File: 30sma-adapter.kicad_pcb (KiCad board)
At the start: 4 copper layers, 34 parts, among them J1 Conn_Coaxial, J10 Conn_Coaxial, J11 Conn_Coaxial, J12 Conn_Coaxial, J13 Conn_Coaxial, J14 Conn_Coaxial, J15 Conn_Coaxial, J16 Conn_Coaxial, J17 Conn_Coaxial, J18 Conn_Coaxial, J19 Conn_Coaxial, J2 Conn_Coaxial, J20 Conn_Coaxial, J21 Conn_Coaxial, J22 Conn_Coaxial, J23 Conn_Coaxial, J24 Conn_Coaxial, J25 Conn_Coaxial, J26 Conn_Coaxial, J27 Conn_Coaxial, J28 Conn_Coaxial, J29 Conn_Coaxial, J3 Conn_Coaxial, J30 Conn_Coaxial, J4 Conn_Coaxial, J5 Conn_Coaxial, J6 Conn_Coaxial, J7 Conn_Coaxial, J8 Conn_Coaxial, J9 Conn_Coaxial

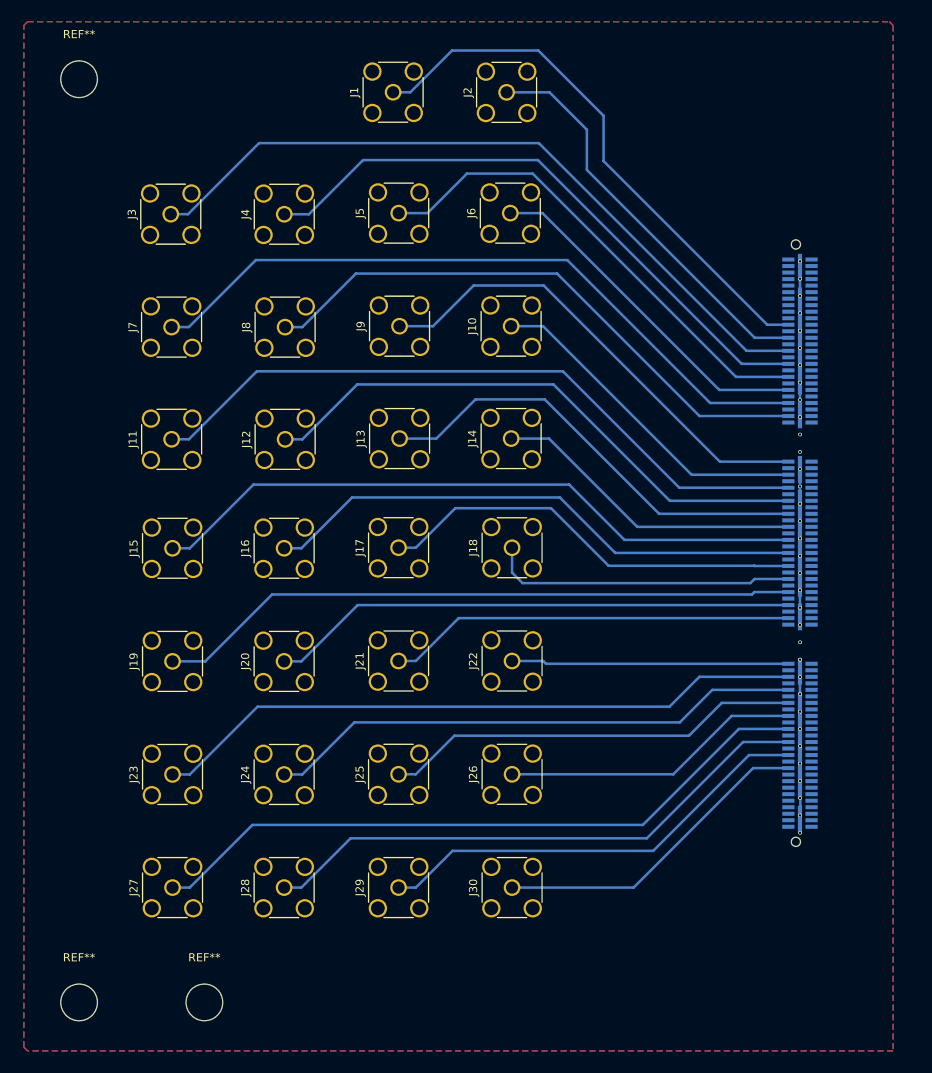
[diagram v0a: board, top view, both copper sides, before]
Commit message: Relabeled silkscreen for the SMA channels to match the ACDC psec channels. Added edge cuts and other silk screening.
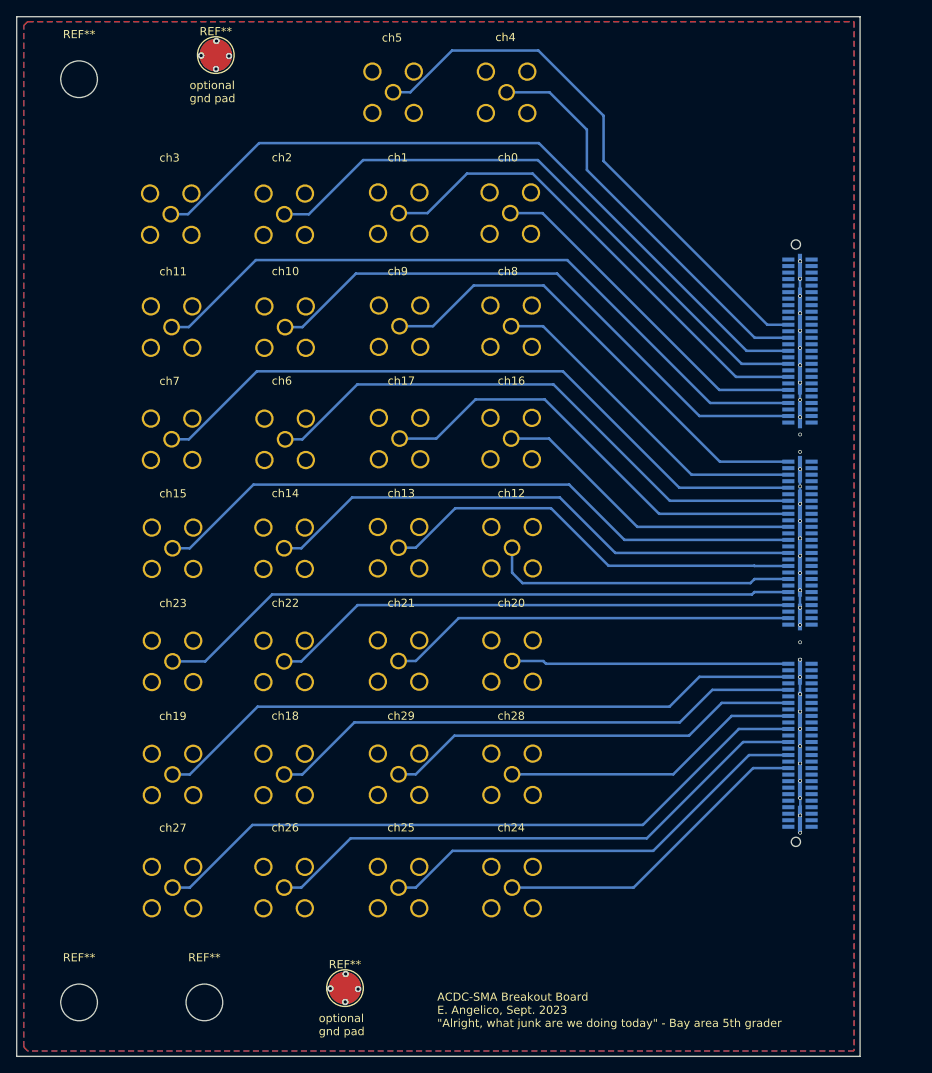
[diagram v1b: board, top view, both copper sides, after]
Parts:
- added REF**: TestPoint_Pad_D4.0mm, TestPoint:TestPoint_Pad_D4.0mm, F.Cu at (124.8, 39.0)
- added REF**: TestPoint_Pad_D4.0mm, TestPoint:TestPoint_Pad_D4.0mm, F.Cu at (140.7, 153.5)
- J1, J10, J11, J12, J13, J14, J15, J16, J17, J18, J19, J2, J20, J21, J22, J23, J24, J25, J26, J27, J28, J29, J3, J30, J4, J5, J6, J7, J8, J9: moved to B.Cu
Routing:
- net /gnd: vias 34 -> 42
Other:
- board outline added: 103.5 x 127.6 mm
- board text added: "ACDC-SMA Breakout Board E. Angelico, Sept. 2023 {dblquote}Alright, what junk are we doing today{dblquote} - Bay area 5th grader"
- board text added: "ch0"
- board text added: "ch1"
- board text added: "ch10"
- board text added: "ch11"
- board text added: "ch12"
- board text added: "ch13"
- board text added: "ch14"
- board text added: "ch15"
- board text added: "ch16"
- board text added: "ch17"
- board text added: "ch18"
- board text added: "ch19"
- board text added: "ch2"
- board text added: "ch20"
- board text added: "ch21"
- board text added: "ch22"
- board text added: "ch23"
- board text added: "ch24"
- board text added: "ch25"
- board text added: "ch26"
- board text added: "ch27"
- board text added: "ch28"
- board text added: "ch29"
- board text added: "ch3"
- board text added: "ch4"
- board text added: "ch5"
- board text added: "ch6"
- board text added: "ch7"
- board text added: "ch8"
- board text added: "ch9"
- board text added: "optional gnd pad"
